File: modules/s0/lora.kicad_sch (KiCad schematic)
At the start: 6 parts, among them J5 Conn_Coaxial, SW2 SW_Push, U5 Ai-Thinker-Ra-01

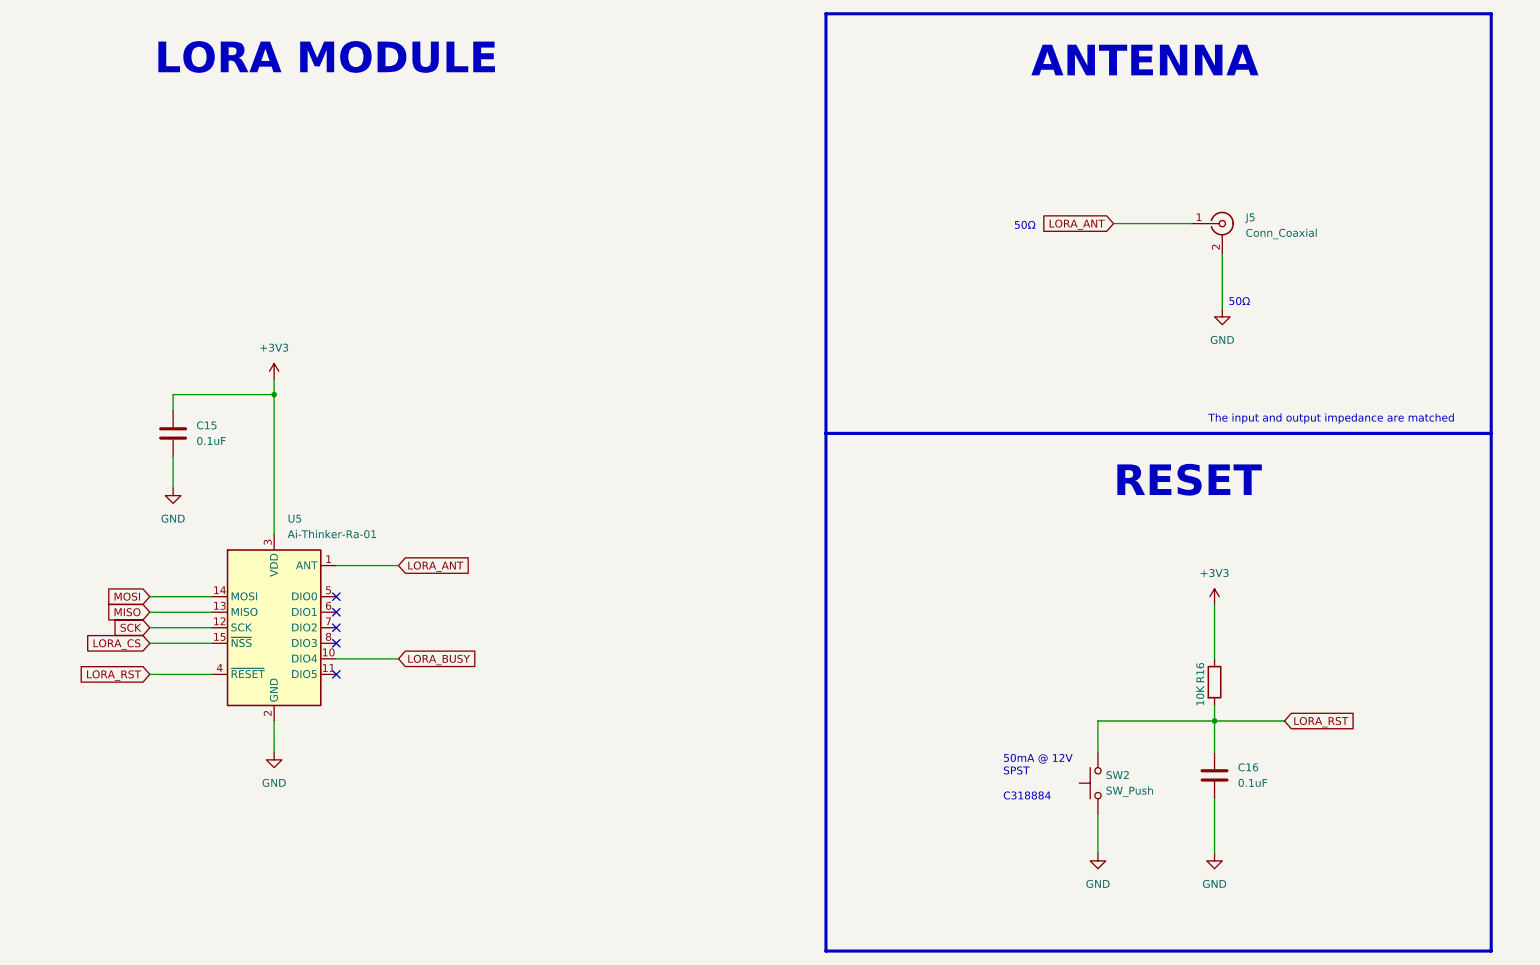
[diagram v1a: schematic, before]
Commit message: chore:Modify BOM in production
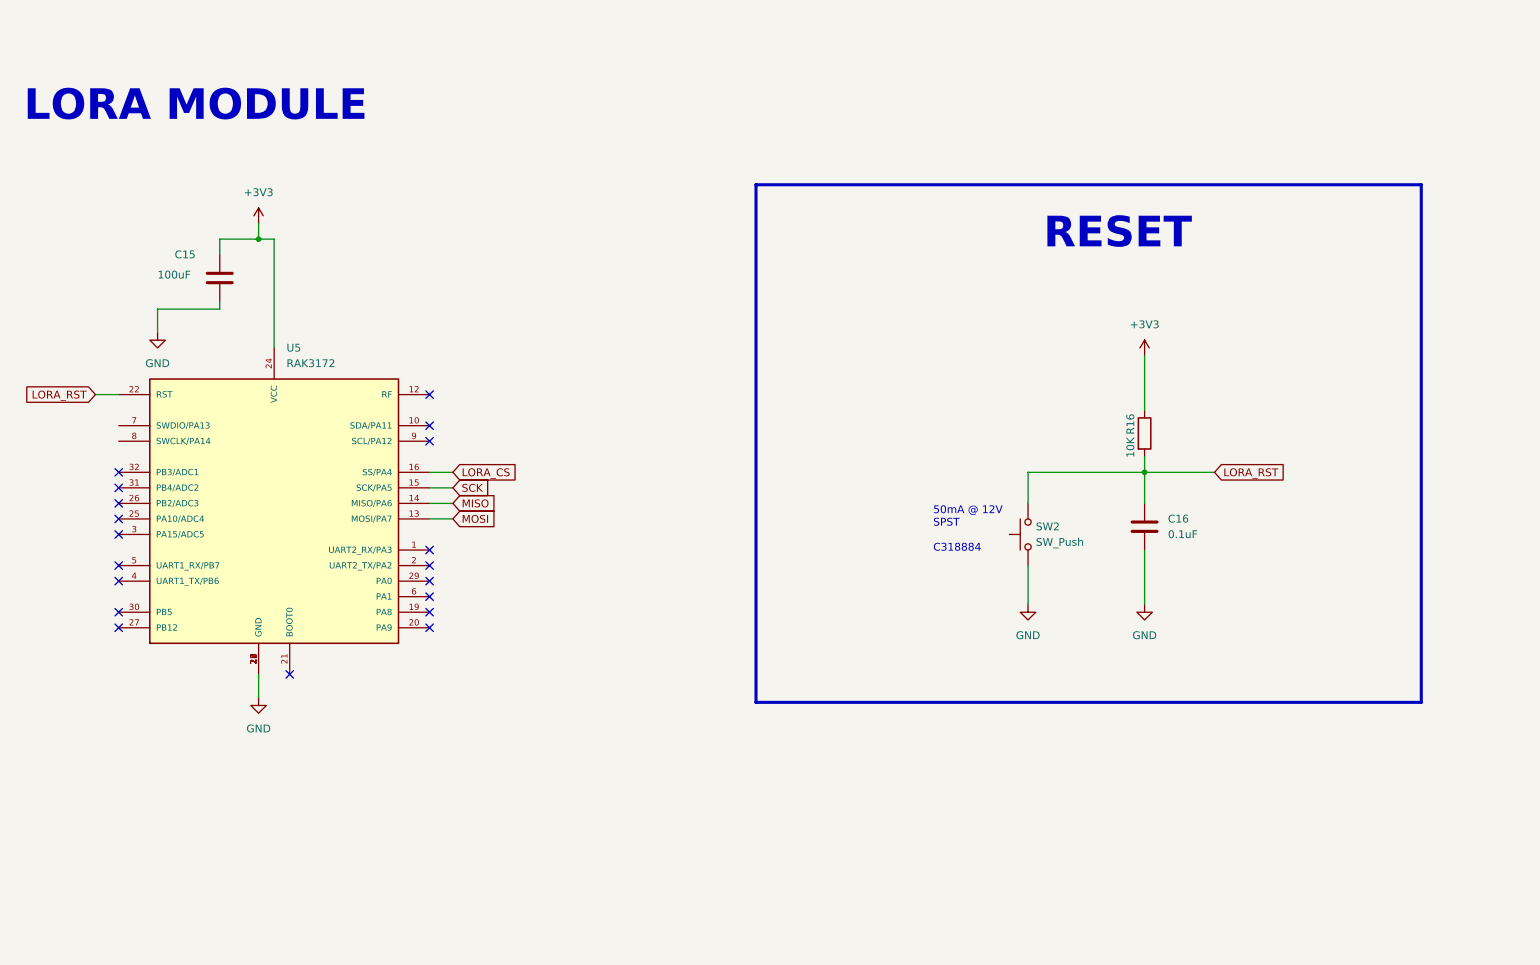
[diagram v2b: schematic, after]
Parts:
- removed J5: Conn_Coaxial, Connector_Coaxial:U.FL_Hirose_U.FL-R-SMT-1_Vertical, symbol Connector:Conn_Coaxial
- removed U5: Ai-Thinker-Ra-01, RF_Module:Ai-Thinker-Ra-01-LoRa, symbol RF_Module:Ai-Thinker-Ra-01
- added U5: RAK3172, Module:RAK3172, symbol BeagleBone Capes:RAK3172
- C15: value 0.1uF -> 100uF
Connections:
- net +3V3: now also U5.24 (VCC)
- net GND: now also U5.11 (GND), U5.17 (GND), U5.18 (GND), U5.23 (GND), U5.28 (GND)
- net LORA_CS: now also U5.16 (SS/PA4)
- net LORA_RST: now also U5.22 (RST)
- net MISO: now also U5.14 (MISO/PA6)
- net MOSI: now also U5.13 (MOSI/PA7)
- net SCK: now also U5.15 (SCK/PA5)
- no-connect marks 5 -> 19
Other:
- note removed: "50Ω"
- note removed: "ANTENNA"
- note removed: "The input and output impedance are matched"
- moved on the sheet: C15, C16, R16, SW2

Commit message: Modified Schematics and BOM
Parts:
- renumbered C15 to C16, C16 to C17, R16 to R15, U5 to U7
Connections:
- net GND: now also U7.21 (BOOT0)
- no-connect marks 19 -> 18
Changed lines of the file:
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@@
+	)
+	(junction
+		(at 83.82 123.19)
+		(diameter 0)
+		(color 0 0 0 0)
 	)
 	(junction
@@
 	)
 	(no_connect
-		(at 88.9 120.65)
-	)
-	(no_connect
 		(at 60.96 110.49)
 	)
@@
 	(wire
 		(pts
+			(xy 88.9 120.65) (xy 88.9 123.19)
+		)
+		(stroke
+			(width 0)
+			(type default)
+		)
+	)
+	(wire
+		(pts
 			(xy 228.6 87.63) (xy 228.6 92.71)
 		)
@@
 	(wire
 		(pts
-			(xy 83.82 120.65) (xy 83.82 124.46)
+			(xy 83.82 120.65) (xy 83.82 123.19)
 		)
 		(stroke
@@
 	(wire
 		(pts
-			(xy 77.47 59.69) (xy 77.47 60.96)
+			(xy 77.47 59.69) (xy 77.47 64.77)
 		)
 		(stroke
@@
 	(wire
 		(pts
+			(xy 88.9 123.19) (xy 83.82 123.19)
+		)
+		(stroke
+			(width 0)
+			(type default)
+		)
+	)
+	(wire
+		(pts
 			(xy 228.6 100.33) (xy 228.6 109.22)
 		)
@@
 	(wire
 		(pts
-			(xy 77.47 60.96) (xy 67.31 60.96)
-		)
-		(stroke
-			(width 0)
-			(type default)
-		)
-	)
-	(wire
-		(pts
 			(xy 228.6 87.63) (xy 240.03 87.63)
 		)
@@
 	(wire
 		(pts
-			(xy 67.31 60.96) (xy 67.31 64.77)
-		)
-		(stroke
-			(width 0)
-			(type default)
-		)
-	)
-	(wire
-		(pts
 			(xy 111.76 92.71) (xy 115.57 92.71)
 		)
@@
 		(pts
 			(xy 86.36 67.31) (xy 86.36 49.53)
+		)
+		(stroke
+			(width 0)
+			(type default)
+		)
+	)
+	(wire
+		(pts
+			(xy 83.82 123.19) (xy 83.82 124.46)
 		)
 		(stroke
@@
 		(dnp no)
 		(fields_autoplaced yes)
-		(property "Reference" "C16"
+		(property "Reference" "C17"
 			(at 232.41 95.2499 0)
 			(effects
@@
 			(project "s0"
 				(path "/9e4c0f80-14bc-451b-8b05-b2f0d1a90e15/a38a5424-854a-4628-876d-ce694417db1d"
-					(reference "C16")
+					(reference "C17")
 					(unit 1)
 				)
@@
 		(dnp no)
 		(fields_autoplaced yes)
-		(property "Reference" "#PWR07"
+		(property "Reference" "#PWR056"
 			(at 83.82 50.8 0)
 			(effects
@@
 			(project ""
 				(path "/9e4c0f80-14bc-451b-8b05-b2f0d1a90e15/a38a5424-854a-4628-876d-ce694417db1d"
-					(reference "#PWR07")
+					(reference "#PWR056")
 					(unit 1)
 				)
@@
 	(symbol
 		(lib_id "power:GND")
-		(at 67.31 64.77 0)
+		(at 77.47 64.77 0)
 		(unit 1)
 		(exclude_from_sim no)
@@
 		(dnp no)
 		(fields_autoplaced yes)
-		(property "Reference" "#PWR011"
-			(at 67.31 71.12 0)
+		(property "Reference" "#PWR055"
+			(at 77.47 71.12 0)
 			(effects
 				(font
@@
 		)
 		(property "Value" "GND"
-			(at 67.31 69.85 0)
+			(at 77.47 69.85 0)
 			(effects
 				(font
@@
 		)
 		(property "Footprint" ""
-			(at 67.31 64.77 0)
+			(at 77.47 64.77 0)
 			(effects
 				(font
@@
 		)
 		(property "Datasheet" ""
-			(at 67.31 64.77 0)
+			(at 77.47 64.77 0)
 			(effects
 				(font
@@
 		)
 		(property "Description" "Power symbol creates a global label with name \"GND\" , ground"
-			(at 67.31 64.77 0)
+			(at 77.47 64.77 0)
 			(effects
 				(font
@@
 			(project "s0"
 				(path "/9e4c0f80-14bc-451b-8b05-b2f0d1a90e15/a38a5424-854a-4628-876d-ce694417db1d"
-					(reference "#PWR011")
+					(reference "#PWR055")
 					(unit 1)
 				)
@@
 		(on_board yes)
 		(dnp no)
-		(property "Reference" "R16"
+		(property "Reference" "R15"
 			(at 226.314 79.756 90)
 			(effects
@@
 			(project "s0"
 				(path "/9e4c0f80-14bc-451b-8b05-b2f0d1a90e15/a38a5424-854a-4628-876d-ce694417db1d"
-					(reference "R16")
+					(reference "R15")
 					(unit 1)
 				)
@@
 		(dnp no)
 		(fields_autoplaced yes)
-		(property "Reference" "#PWR013"
+		(property "Reference" "#PWR060"
 			(at 228.6 115.57 0)
 			(effects
@@
 			(project "s0"
 				(path "/9e4c0f80-14bc-451b-8b05-b2f0d1a90e15/a38a5424-854a-4628-876d-ce694417db1d"
-					(reference "#PWR013")
+					(reference "#PWR060")
 					(unit 1)
 				)
@@
 		(dnp no)
 		(fields_autoplaced yes)
-		(property "Reference" "#PWR010"
+		(property "Reference" "#PWR058"
 			(at 209.55 115.57 0)
 			(effects
@@
 			(project "s0"
 				(path "/9e4c0f80-14bc-451b-8b05-b2f0d1a90e15/a38a5424-854a-4628-876d-ce694417db1d"
-					(reference "#PWR010")
+					(reference "#PWR058")
 					(unit 1)
 				)
@@
 		(on_board yes)
 		(dnp no)
-		(property "Reference" "C15"
+		(property "Reference" "C16"
 			(at 70.104 52.07 0)
 			(effects
@@
 			)
 		)
-		(property "Description" "Unpolarized capacitor"
+		(property "Description" "16V 100nF X7R ±10% 0402 Multilayer Ceramic Capacitors MLCC - SMD/SMT ROHS"
 			(at 77.47 55.88 0)
 			(effects
@@
 			(project "s0"
 				(path "/9e4c0f80-14bc-451b-8b05-b2f0d1a90e15/a38a5424-854a-4628-876d-ce694417db1d"
-					(reference "C15")
+					(reference "C16")
 					(unit 1)
 				)
@@
 		(dnp no)
 		(fields_autoplaced yes)
-		(property "Reference" "#PWR012"
+		(property "Reference" "#PWR059"
 			(at 228.6 72.39 0)
 			(effects
@@
 			(project "s0"
 				(path "/9e4c0f80-14bc-451b-8b05-b2f0d1a90e15/a38a5424-854a-4628-876d-ce694417db1d"
-					(reference "#PWR012")
+					(reference "#PWR059")
 					(unit 1)
 				)
@@
 		(dnp no)
 		(fields_autoplaced yes)
-		(property "Reference" "U5"
+		(property "Reference" "U7"
 			(at 88.3794 67.31 0)
 			(effects
@@
 			(project ""
 				(path "/9e4c0f80-14bc-451b-8b05-b2f0d1a90e15/a38a5424-854a-4628-876d-ce694417db1d"
-					(reference "U5")
+					(reference "U7")
 					(unit 1)
 				)
@@
 		(dnp no)
 		(fields_autoplaced yes)
-		(property "Reference" "#PWR03"
+		(property "Reference" "#PWR057"
 			(at 83.82 130.81 0)
 			(effects
@@
 			(project "s0"
 				(path "/9e4c0f80-14bc-451b-8b05-b2f0d1a90e15/a38a5424-854a-4628-876d-ce694417db1d"
-					(reference "#PWR03")
+					(reference "#PWR057")
 					(unit 1)
 				)

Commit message: chore: route the board with changes
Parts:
- U7: footprint Module:RAK3172 -> modules:RAK3172
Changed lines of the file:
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@@
 			)
 		)
-		(property "Footprint" "Module:RAK3172"
+		(property "Footprint" "modules:RAK3172"
 			(at 67.056 123.19 0)
 			(effects
